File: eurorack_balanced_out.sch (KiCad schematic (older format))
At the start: 33 parts, among them J1 Conn_01x02, J2 Conn_01x02, J3 Conn_02x05_Odd_Even, J4 AudioJack3, J5 AudioJack3, U1 THAT1646W16, U2 THAT1646W16

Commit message: update schematic, add input buffer
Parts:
- removed U1, U2: THAT1646W16, Package_SO:SOIC-16W_7.5x10.3mm_P1.27mm, symbol patchut:THAT1646W16
- added C3, C4: 100n, Capacitor_SMD:C_0805_2012Metric_Pad1.15x1.40mm_HandSolder, symbol Device:C_Small
- added D2, D4: BAV99, Package_TO_SOT_SMD:SOT-23, symbol Diode:BAV99
- added U1: TL072, Package_SO:SO-8_5.3x6.2mm_P1.27mm, symbol Amplifier_Operational:TL072
- added U2, U3: THAT1646S08, Package_SO:SOIC-8_3.9x4.9mm_P1.27mm, symbol Eurorack:THAT1646S08
- renumbered C4 to C10, C13 to C11, C14 to C12, C9 to C13, C10 to C14, C11 to C15, C12 to C16, C3 to C9, D4 to D5, D2 to D6, J3 to J1, J1 to J2, J2 to J3
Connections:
- wire segments 141 -> 152
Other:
- moved on the sheet: C1, C2, D5, D6, J1, R1, R2, R3, R4

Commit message: increase input impedance
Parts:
- C10, C9: footprint Capacitor_SMD:C_0805_2012Metric_Pad1.15x1.40mm_HandSolder -> Capacitor_SMD:C_0805_2012Metric_Pad1.18x1.45mm_HandSolder
- R1, R2: value 3.9k -> 39k
- R3, R4: value 1.2k -> 12k
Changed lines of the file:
@@
 P 3300 1850
 F 0 "R3" H 3241 1804 50  0000 R CNN
-F 1 "1.2k" H 3241 1895 50  0000 R CNN
+F 1 "12k" H 3241 1895 50  0000 R CNN
 F 2 "Resistor_SMD:R_0805_2012Metric_Pad1.15x1.40mm_HandSolder" H 3300 1850 50  0001 C CNN
 F 3 "~" H 3300 1850 50  0001 C CNN
@@
 P 3150 1700
 F 0 "R1" V 2954 1700 50  0000 C CNN
-F 1 "3.9k" V 3045 1700 50  0000 C CNN
+F 1 "39k" V 3045 1700 50  0000 C CNN
 F 2 "Resistor_SMD:R_0805_2012Metric_Pad1.15x1.40mm_HandSolder" H 3150 1700 50  0001 C CNN
 F 3 "~" H 3150 1700 50  0001 C CNN
@@
 P 3300 4350
 F 0 "R4" H 3241 4304 50  0000 R CNN
-F 1 "1.2k" H 3241 4395 50  0000 R CNN
+F 1 "12k" H 3241 4395 50  0000 R CNN
 F 2 "Resistor_SMD:R_0805_2012Metric_Pad1.15x1.40mm_HandSolder" H 3300 4350 50  0001 C CNN
 F 3 "~" H 3300 4350 50  0001 C CNN
@@
 P 3150 4200
 F 0 "R2" V 2954 4200 50  0000 C CNN
-F 1 "3.9k" V 3045 4200 50  0000 C CNN
+F 1 "39k" V 3045 4200 50  0000 C CNN
 F 2 "Resistor_SMD:R_0805_2012Metric_Pad1.15x1.40mm_HandSolder" H 3150 4200 50  0001 C CNN
 F 3 "~" H 3150 4200 50  0001 C CNN
@@
 F 0 "C9" V 5198 6500 50  0000 C CNN
 F 1 "100n" V 5289 6500 50  0000 C CNN
-F 2 "Capacitor_SMD:C_0805_2012Metric_Pad1.15x1.40mm_HandSolder" H 5488 6350 50  0001 C CNN
+F 2 "Capacitor_SMD:C_0805_2012Metric_Pad1.18x1.45mm_HandSolder" H 5488 6350 50  0001 C CNN
 F 3 "~" H 5450 6500 50  0001 C CNN
 F 4 "80-C0805C104K5RACLR" V 5450 6500 50  0001 C CNN "Mouser"
@@
 F 0 "C10" V 5198 6800 50  0000 C CNN
 F 1 "100n" V 5289 6800 50  0000 C CNN
-F 2 "Capacitor_SMD:C_0805_2012Metric_Pad1.15x1.40mm_HandSolder" H 5488 6650 50  0001 C CNN
+F 2 "Capacitor_SMD:C_0805_2012Metric_Pad1.18x1.45mm_HandSolder" H 5488 6650 50  0001 C CNN
 F 3 "~" H 5450 6800 50  0001 C CNN
 F 4 "80-C0805C104K5RACLR" V 5450 6800 50  0001 C CNN "Mouser"

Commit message: set input and output jacks
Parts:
- removed J2, J3: Conn_01x02, Connector_PinHeader_2.54mm:PinHeader_1x02_P2.54mm_Vertical, symbol Connector_Generic:Conn_01x02
- added J2, J3: AudioJack2_SwitchT, Connector_Audio:Jack_3.5mm_QingPu_WQP-PJ398SM_Vertical_CircularHoles, symbol Connector:AudioJack2_SwitchT
- J4, J5: footprint Connector_Audio:Jack_6.35mm_Neutrik_NJ3FD-V_Vertical -> Connector_Audio:Jack_3.5mm_QingPu_WQP-PJ398SM_Vertical_CircularHoles
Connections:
- wire segments 152 -> 161
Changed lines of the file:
@@
 $EndComp
 $Comp
-L Connector_Generic:Conn_01x02 J2
-U 1 1 5EC8DDA9
-P 2600 1700
-F 0 "J2" H 2518 1917 50  0000 C CNN
-F 1 "Conn_01x02" H 2518 1826 50  0000 C CNN
-F 2 "Connector_PinHeader_2.54mm:PinHeader_1x02_P2.54mm_Vertical" H 2600 1700 50  0001 C CNN
-F 3 "~" H 2600 1700 50  0001 C CNN
-F 4 "200-TSW10207TS" H 2600 1700 50  0001 C CNN "Mouser"
-	1    2600 1700
-	-1   0    0    -1
-$EndComp
-$Comp
-L power:GND #PWR010
+L power:GND #PWR011
 U 1 1 5ECC7C45
 P 6850 2150
-F 0 "#PWR010" H 6850 1900 50  0001 C CNN
+F 0 "#PWR011" H 6850 1900 50  0001 C CNN
 F 1 "GND" H 6855 1977 50  0000 C CNN
 F 2 "" H 6850 2150 50  0001 C CNN
@@
 F 0 "J4" H 7370 1633 50  0000 R CNN
 F 1 "AudioJack3" H 7370 1724 50  0000 R CNN
-F 2 "Connector_Audio:Jack_6.35mm_Neutrik_NJ3FD-V_Vertical" H 7650 1700 50  0001 C CNN
+F 2 "Connector_Audio:Jack_3.5mm_QingPu_WQP-PJ398SM_Vertical_CircularHoles" H 7650 1700 50  0001 C CNN
 F 3 "~" H 7650 1700 50  0001 C CNN
 F 4 "568-NJ3FD-V" H 7650 1700 50  0001 C CNN "Mouser"
@@
 Vcc
 $Comp
-L Connector_Generic:Conn_01x02 J3
-U 1 1 5ECBF51E
-P 2600 4200
-F 0 "J3" H 2518 4417 50  0000 C CNN
-F 1 "Conn_01x02" H 2518 4326 50  0000 C CNN
-F 2 "Connector_PinHeader_2.54mm:PinHeader_1x02_P2.54mm_Vertical" H 2600 4200 50  0001 C CNN
-F 3 "~" H 2600 4200 50  0001 C CNN
-F 4 "200-TSW10207TS" H 2600 4200 50  0001 C CNN "Mouser"
-	1    2600 4200
-	-1   0    0    -1
-$EndComp
-$Comp
-L power:GND #PWR011
+L power:GND #PWR012
 U 1 1 5ECBF53E
 P 6850 4650
-F 0 "#PWR011" H 6850 4400 50  0001 C CNN
+F 0 "#PWR012" H 6850 4400 50  0001 C CNN
 F 1 "GND" H 6855 4477 50  0000 C CNN
 F 2 "" H 6850 4650 50  0001 C CNN
@@
 F 0 "J5" H 7370 4133 50  0000 R CNN
 F 1 "AudioJack3" H 7370 4224 50  0000 R CNN
-F 2 "Connector_Audio:Jack_6.35mm_Neutrik_NJ3FD-V_Vertical" H 7650 4200 50  0001 C CNN
+F 2 "Connector_Audio:Jack_3.5mm_QingPu_WQP-PJ398SM_Vertical_CircularHoles" H 7650 4200 50  0001 C CNN
 F 3 "~" H 7650 4200 50  0001 C CNN
 F 4 "568-NJ3FD-V" H 7650 4200 50  0001 C CNN "Mouser"
@@
 $EndComp
 $Comp
-L power:GND #PWR06
+L power:GND #PWR07
 U 1 1 5EC6F187
 P 3600 6650
-F 0 "#PWR06" H 3600 6400 50  0001 C CNN
+F 0 "#PWR07" H 3600 6400 50  0001 C CNN
 F 1 "GND" H 3605 6477 50  0000 C CNN
 F 2 "" H 3600 6650 50  0001 C CNN
@@
 Vee
 $Comp
-L power:GND #PWR04
+L power:GND #PWR05
 U 1 1 5EC6D54F
 P 3300 2000
-F 0 "#PWR04" H 3300 1750 50  0001 C CNN
+F 0 "#PWR05" H 3300 1750 50  0001 C CNN
 F 1 "GND" H 3305 1827 50  0000 C CNN
 F 2 "" H 3300 2000 50  0001 C CNN
@@
 	-1   0    0    1
 $EndComp
-Wire Wire Line
-	2800 1700 3050 1700
 $Comp
 L Device:R_Small R1
@@
 	3250 1700 3300 1700
 $Comp
-L power:GND #PWR05
+L power:GND #PWR06
 U 1 1 5ED56EC8
 P 3300 4500
-F 0 "#PWR05" H 3300 4250 50  0001 C CNN
+F 0 "#PWR06" H 3300 4250 50  0001 C CNN
 F 1 "GND" H 3305 4327 50  0000 C CNN
 F 2 "" H 3300 4500 50  0001 C CNN
@@
 	-1   0    0    1
 $EndComp
-Wire Wire Line
-	2800 4200 3050 4200
 $Comp
 L Device:R_Small R2
@@
 	6350 6650 6350 6700
 $Comp
-L power:GND #PWR09
+L power:GND #PWR010
 U 1 1 5ED856DA
 P 6350 6700
-F 0 "#PWR09" H 6350 6450 50  0001 C CNN
+F 0 "#PWR010" H 6350 6450 50  0001 C CNN
 F 1 "GND" H 6355 6527 50  0000 C CNN
 F 2 "" H 6350 6700 50  0001 C CNN
@@
 L power:GND #PWR03
 U 1 1 608EA7CA
-P 2850 4350
-F 0 "#PWR03" H 2850 4100 50  0001 C CNN
-F 1 "GND" H 2855 4177 50  0000 C CNN
-F 2 "" H 2850 4350 50  0001 C CNN
-F 3 "" H 2850 4350 50  0001 C CNN
-	1    2850 4350
-	1    0    0    -1
-$EndComp
-Wire Wire Line
-	2800 4300 2850 4300
-Wire Wire Line
-	2850 4300 2850 4350
+P 2450 4350
+F 0 "#PWR03" H 2450 4100 50  0001 C CNN
+F 1 "GND" H 2455 4177 50  0000 C CNN
+F 2 "" H 2450 4350 50  0001 C CNN
+F 3 "" H 2450 4350 50  0001 C CNN
+	1    2450 4350
+	1    0    0    -1
+$EndComp
+Wire Wire Line
+	2400 4300 2450 4300
+Wire Wire Line
+	2450 4300 2450 4350
 Wire Wire Line
 	3300 4200 3650 4200
 Connection ~ 3300 4200
 $Comp
-L power:GND #PWR08
+L power:GND #PWR09
 U 1 1 608FB7E9
 P 4450 4350
-F 0 "#PWR08" H 4450 4100 50  0001 C CNN
+F 0 "#PWR09" H 4450 4100 50  0001 C CNN
 F 1 "GND" H 4455 4177 50  0000 C CNN
 F 2 "" H 4450 4350 50  0001 C CNN
@@
 L power:GND #PWR02
 U 1 1 609827C5
-P 2850 1850
-F 0 "#PWR02" H 2850 1600 50  0001 C CNN
-F 1 "GND" H 2855 1677 50  0000 C CNN
-F 2 "" H 2850 1850 50  0001 C CNN
-F 3 "" H 2850 1850 50  0001 C CNN
-	1    2850 1850
-	1    0    0    -1
-$EndComp
-Wire Wire Line
-	2800 1800 2850 1800
-Wire Wire Line
-	2850 1800 2850 1850
+P 2450 1850
+F 0 "#PWR02" H 2450 1600 50  0001 C CNN
+F 1 "GND" H 2455 1677 50  0000 C CNN
+F 2 "" H 2450 1850 50  0001 C CNN
+F 3 "" H 2450 1850 50  0001 C CNN
+	1    2450 1850
+	1    0    0    -1
+$EndComp
+Wire Wire Line
+	2400 1800 2450 1800
+Wire Wire Line
+	2450 1800 2450 1850
 Wire Wire Line
 	3300 1700 3650 1700
 Connection ~ 3300 1700
 $Comp
-L power:GND #PWR07
+L power:GND #PWR08
 U 1 1 609B209F
 P 4450 1850
-F 0 "#PWR07" H 4450 1600 50  0001 C CNN
+F 0 "#PWR08" H 4450 1600 50  0001 C CNN
 F 1 "GND" H 4455 1677 50  0000 C CNN
 F 2 "" H 4450 1850 50  0001 C CNN
@@
 	1    0    0    -1
 $EndComp
+$Comp
+L Connector:AudioJack2_SwitchT J2
+U 1 1 608D5F68
+P 2200 1700
+F 0 "J2" H 2021 1633 50  0000 R CNN
+F 1 "AudioJack2_SwitchT" H 2021 1724 50  0000 R CNN
+F 2 "Connector_Audio:Jack_3.5mm_QingPu_WQP-PJ398SM_Vertical_CircularHoles" H 2200 1700 50  0001 C CNN
+F 3 "~" H 2200 1700 50  0001 C CNN
+	1    2200 1700
+	1    0    0    1
+$EndComp
+$Comp
+L Connector:AudioJack2_SwitchT J3
+U 1 1 608E218C
+P 2200 4200
+F 0 "J3" H 2021 4133 50  0000 R CNN
+F 1 "AudioJack2_SwitchT" H 2021 4224 50  0000 R CNN
+F 2 "Connector_Audio:Jack_3.5mm_QingPu_WQP-PJ398SM_Vertical_CircularHoles" H 2200 4200 50  0001 C CNN
+F 3 "~" H 2200 4200 50  0001 C CNN
+	1    2200 4200
+	1    0    0    1
+$EndComp
+Wire Wire Line
+	2400 4200 3050 4200
+Wire Wire Line
+	2400 1700 2800 1700
+Wire Wire Line
+	2800 1700 2800 2800
+Wire Wire Line
+	2800 2800 2450 2800
+Wire Wire Line
+	2450 2800 2450 4100
+Wire Wire Line
+	2450 4100 2400 4100
+Connection ~ 2800 1700
+Wire Wire Line
+	2800 1700 3050 1700
+$Comp
+L power:GND #PWR04
+U 1 1 60927C85
+P 2700 1400
+F 0 "#PWR04" H 2700 1150 50  0001 C CNN
+F 1 "GND" H 2705 1227 50  0000 C CNN
+F 2 "" H 2700 1400 50  0001 C CNN
+F 3 "" H 2700 1400 50  0001 C CNN
+	1    2700 1400
+	1    0    0    -1
+$EndComp
+Wire Wire Line
+	2400 1600 2450 1600
+Wire Wire Line
+	2450 1600 2450 1350
+Wire Wire Line
+	2450 1350 2700 1350
+Wire Wire Line
+	2700 1350 2700 1400
 $EndSCHEMATC

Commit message: Cleanup of Schematic
Separated input and output clamps
Improved formatting
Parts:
- C10: renamed from C13; footprint Capacitor_SMD:C_0805_2012Metric_Pad1.15x1.40mm_HandSolder -> Capacitor_SMD:C_0805_2012Metric_Pad1.18x1.45mm_HandSolder
- C11: renamed from C15; footprint Capacitor_SMD:C_0805_2012Metric_Pad1.15x1.40mm_HandSolder -> Capacitor_SMD:C_0805_2012Metric_Pad1.18x1.45mm_HandSolder
- C14: footprint Capacitor_SMD:C_0805_2012Metric_Pad1.15x1.40mm_HandSolder -> Capacitor_SMD:C_0805_2012Metric_Pad1.18x1.45mm_HandSolder
- C15: renamed from C16; footprint Capacitor_SMD:C_0805_2012Metric_Pad1.15x1.40mm_HandSolder -> Capacitor_SMD:C_0805_2012Metric_Pad1.18x1.45mm_HandSolder
- C2: renamed from C3; footprint Capacitor_SMD:C_0805_2012Metric_Pad1.15x1.40mm_HandSolder -> Capacitor_SMD:C_0805_2012Metric_Pad1.18x1.45mm_HandSolder
- C4: renamed from C11; footprint Capacitor_SMD:C_0805_2012Metric_Pad1.15x1.40mm_HandSolder -> Capacitor_SMD:C_0805_2012Metric_Pad1.18x1.45mm_HandSolder
- C6: renamed from C4; footprint Capacitor_SMD:C_0805_2012Metric_Pad1.15x1.40mm_HandSolder -> Capacitor_SMD:C_0805_2012Metric_Pad1.18x1.45mm_HandSolder
- C8: renamed from C12; footprint Capacitor_SMD:C_0805_2012Metric_Pad1.15x1.40mm_HandSolder -> Capacitor_SMD:C_0805_2012Metric_Pad1.18x1.45mm_HandSolder
- FB1, FB2, FB3, FB4, R1, R4: footprint Resistor_SMD:R_0805_2012Metric_Pad1.15x1.40mm_HandSolder -> Resistor_SMD:R_0805_2012Metric_Pad1.20x1.40mm_HandSolder
- J1: value Conn_02x05_Odd_Even -> Eurorack_ribbon
- J2: value AudioJack2_SwitchT -> Audio_in_1
- J3: renamed from J4; value AudioJack3 -> Balanced_out_1
- J4: renamed from J3; value AudioJack2_SwitchT -> Audio_in_2
- J5: value AudioJack3 -> Balanced_out_2
- R2: renamed from R3; footprint Resistor_SMD:R_0805_2012Metric_Pad1.15x1.40mm_HandSolder -> Resistor_SMD:R_0805_2012Metric_Pad1.20x1.40mm_HandSolder
- R3: renamed from R2; footprint Resistor_SMD:R_0805_2012Metric_Pad1.15x1.40mm_HandSolder -> Resistor_SMD:R_0805_2012Metric_Pad1.20x1.40mm_HandSolder
- U2, U3: symbol Eurorack:THAT1646S08 -> patchut:THAT1646S08
- renumbered C6 to C12, C7 to C13, C8 to C16, C9 to C3, C2 to C5, C10 to C7, C5 to C9
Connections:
- net Clamp_out_1_P: now reaches C9.1, D3.3 (K), FB1.2, U2.8 (+OUT)
- net Clamp_out_1_N: now reaches C12.1, D4.3 (K), FB2.2, U2.1 (-OUT)
- net Clamp_out_2_P: now reaches C13.1, D5.3 (K), FB3.2, U3.8 (+OUT)
- net Clamp_out_2_N: now reaches C16.1, D6.3 (K), FB4.2, U3.1 (-OUT)
- net Clamp_in_1: now reaches D1.3 (K), R1.1, R2.2, U1.3 (+)
- net Clamp_in_2: now reaches D2.3 (K), R3.1, R4.2, U1.5 (+)
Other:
- note added: "Input Voltage Protection Clamps"
- note added: "Output Voltage Protection Clamps"
- note added: "Power Filtering"
- note added: "Power Input"
- moved on the sheet: C1, C10, C11, C12, C13, C14, C15, C16, C2, C3, C4, C5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

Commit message: fix typo in THAT1646 symbol reference
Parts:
- removed U2, U3: THAT1646S08, Package_SO:SOIC-8_3.9x4.9mm_P1.27mm, symbol patchut:THAT1646S08
- added U2, U3: THAT1646S08, Package_SO:SOIC-8_3.9x4.9mm_P1.27mm, symbol patchnut:THAT1646S08
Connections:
- net Clamp_out_1_N: now also U2.1 (-OUT)
- net Clamp_out_1_P: now also U2.8 (+OUT)
- net Clamp_out_2_N: now also U3.1 (-OUT)
- net Clamp_out_2_P: now also U3.8 (+OUT)
- net GND: now also U2.3 (GND), U3.3 (GND)
- net Vcc: now also U2.6 (V+), U3.6 (V+)
- net Vee: now also U2.5 (V-), U3.5 (V-)
- net at C12.2: now also U2.2 (-SNS)
- net at C9.2: now also U2.7 (+SNS)
- net at C13.2: now also U3.7 (+SNS)
- net at C16.2: now also U3.2 (-SNS)
- net at U1.1, U1.2 (-): now also U2.4 (IN)
- net at U1.6 (-), U1.7: now also U3.4 (IN)
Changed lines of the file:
@@
 	8150 1100 8150 1050
-$Comp
-L patchut:THAT1646S08 U2
-U 1 1 608C03F2
-P 4550 3600
-F 0 "U2" H 4894 3646 50  0000 L CNN
-F 1 "THAT1646S08" H 4894 3555 50  0000 L CNN
-F 2 "Package_SO:SOIC-8_3.9x4.9mm_P1.27mm" H 4500 3050 50  0001 C CNN
-F 3 "http://www.thatcorp.com/datashts/THAT_1606-1646_Datasheet.pdf" H 4400 3950 50  0001 C CNN
-	1    4550 3600
-	1    0    0    -1
-$EndComp
-$Comp
-L patchut:THAT1646S08 U3
-U 1 1 608DF4CF
-P 4550 5300
-F 0 "U3" H 4894 5346 50  0000 L CNN
-F 1 "THAT1646S08" H 4894 5255 50  0000 L CNN
-F 2 "Package_SO:SOIC-8_3.9x4.9mm_P1.27mm" H 4500 4750 50  0001 C CNN
-F 3 "http://www.thatcorp.com/datashts/THAT_1606-1646_Datasheet.pdf" H 4400 5650 50  0001 C CNN
-	1    4550 5300
-	1    0    0    -1
-$EndComp
 $Comp
 L Connector:AudioJack2_SwitchT J2
@@
 Wire Notes Line
 	5600 2050 3100 2050
+$Comp
+L patchnut:THAT1646S08 U2
+U 1 1 6098E315
+P 4550 3600
+F 0 "U2" H 4894 3646 50  0000 L CNN
+F 1 "THAT1646S08" H 4894 3555 50  0000 L CNN
+F 2 "Package_SO:SOIC-8_3.9x4.9mm_P1.27mm" H 4500 3050 50  0001 C CNN
+F 3 "http://www.thatcorp.com/datashts/THAT_1606-1646_Datasheet.pdf" H 4400 3950 50  0001 C CNN
+	1    4550 3600
+	1    0    0    -1
+$EndComp
+$Comp
+L patchnut:THAT1646S08 U3
+U 1 1 60996725
+P 4550 5300
+F 0 "U3" H 4894 5346 50  0000 L CNN
+F 1 "THAT1646S08" H 4894 5255 50  0000 L CNN
+F 2 "Package_SO:SOIC-8_3.9x4.9mm_P1.27mm" H 4500 4750 50  0001 C CNN
+F 3 "http://www.thatcorp.com/datashts/THAT_1606-1646_Datasheet.pdf" H 4400 5650 50  0001 C CNN
+	1    4550 5300
+	1    0    0    -1
+$EndComp
 $EndSCHEMATC

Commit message: use thonkycon TRS footprint for outputs
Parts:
- J3, J5: footprint Connector_Audio:Jack_3.5mm_QingPu_WQP-PJ398SM_Vertical_CircularHoles -> patchnut:Jack_3.5mm_ThonkiConn_TRS-PJ366ST_Vertical
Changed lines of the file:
@@
 F 0 "J3" H 7900 3800 50  0000 R CNN
 F 1 "Balanced_out_1" H 7950 3350 50  0000 R CNN
-F 2 "Connector_Audio:Jack_3.5mm_QingPu_WQP-PJ398SM_Vertical_CircularHoles" H 7800 3600 50  0001 C CNN
+F 2 "patchnut:Jack_3.5mm_ThonkiConn_TRS-PJ366ST_Vertical" H 7800 3600 50  0001 C CNN
 F 3 "~" H 7800 3600 50  0001 C CNN
 F 4 "568-NJ3FD-V" H 7800 3600 50  0001 C CNN "Mouser"
@@
 F 0 "J5" H 7900 5500 50  0000 R CNN
 F 1 "Balanced_out_2" H 7950 5050 50  0000 R CNN
-F 2 "Connector_Audio:Jack_3.5mm_QingPu_WQP-PJ398SM_Vertical_CircularHoles" H 7800 5300 50  0001 C CNN
+F 2 "patchnut:Jack_3.5mm_ThonkiConn_TRS-PJ366ST_Vertical" H 7800 5300 50  0001 C CNN
 F 3 "~" H 7800 5300 50  0001 C CNN
 F 4 "568-NJ3FD-V" H 7800 5300 50  0001 C CNN "Mouser"

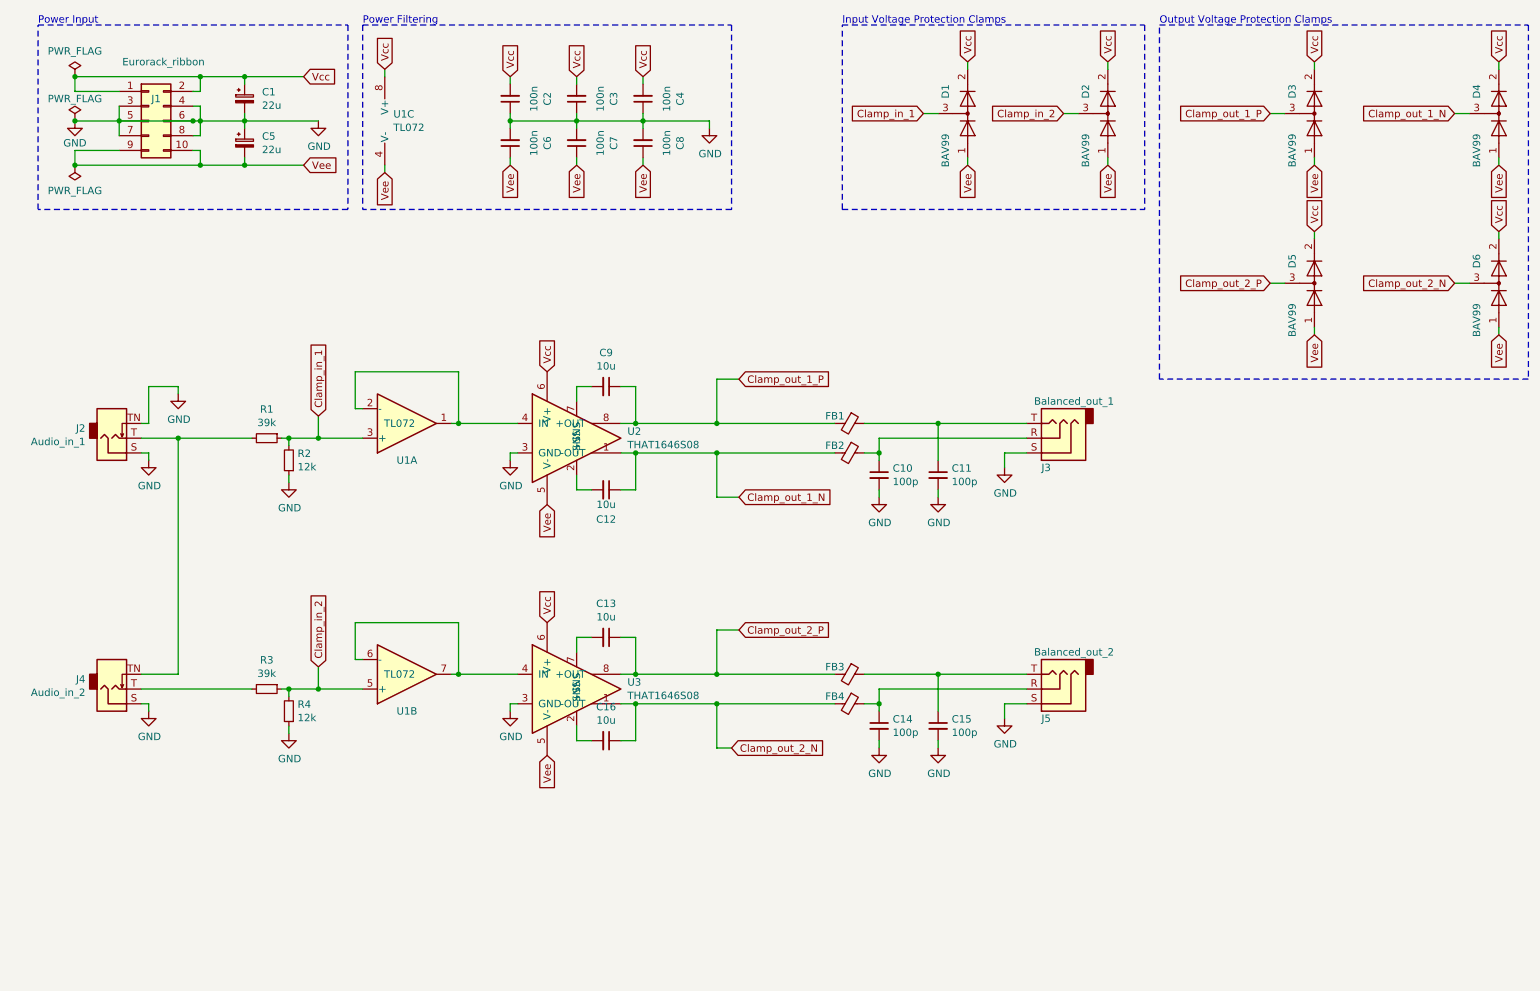
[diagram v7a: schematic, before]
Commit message: remove clamps from schematic
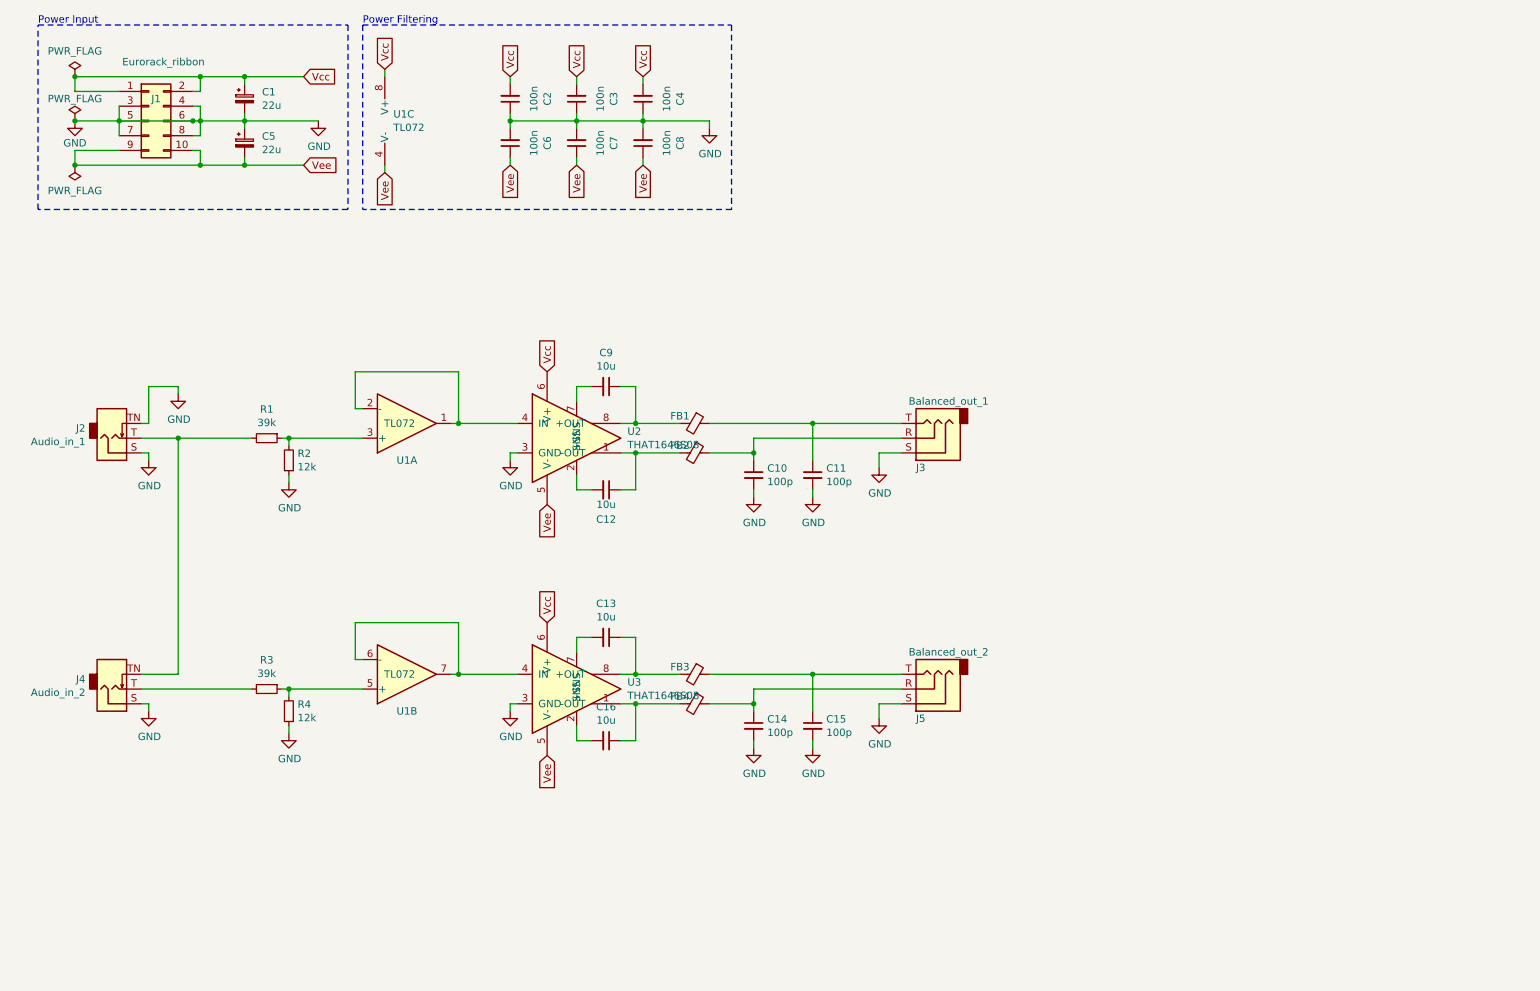
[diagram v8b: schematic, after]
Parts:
- removed D1, D2, D3, D4, D5, D6: BAV99, Package_TO_SOT_SMD:SOT-23, symbol Diode:BAV99
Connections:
- net Clamp_in_1: no longer names the net of R1.1, R2.2, U1.3 (+)
- net Clamp_in_2: no longer names the net of R3.1, R4.2, U1.5 (+)
- net Clamp_out_1_N: no longer names the net of C12.1, FB2.2, U2.1 (-OUT)
- net Clamp_out_1_P: no longer names the net of C9.1, FB1.2, U2.8 (+OUT)
- net Clamp_out_2_N: no longer names the net of C16.1, FB4.2, U3.1 (-OUT)
- net Clamp_out_2_P: no longer names the net of C13.1, FB3.2, U3.8 (+OUT)
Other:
- note removed: "Input Voltage Protection Clamps"
- note removed: "Output Voltage Protection Clamps"
- moved on the sheet: C10, C11, C14, C15, FB1, FB2, FB3, FB4, J3, J5
